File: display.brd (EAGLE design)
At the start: 64.5 x 30.8 mm, 9 parts

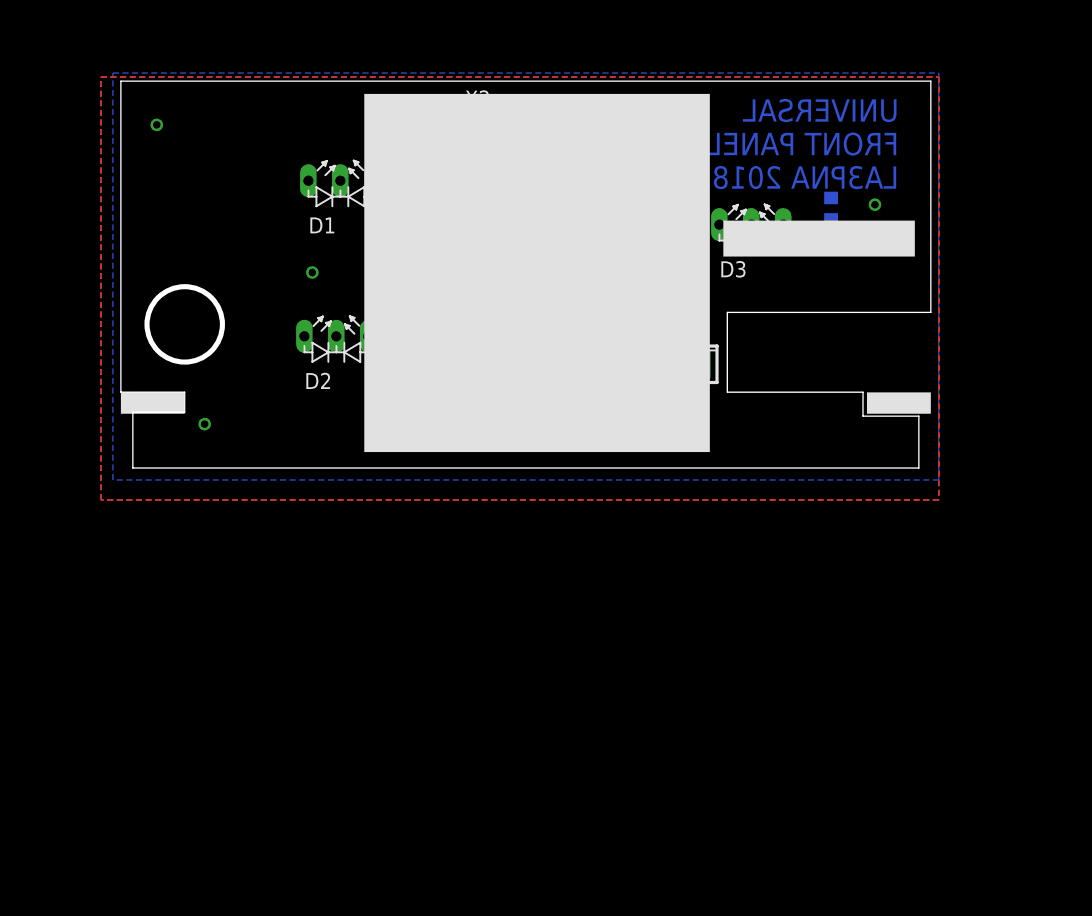
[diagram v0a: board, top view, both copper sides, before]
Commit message: front panel board made to fit
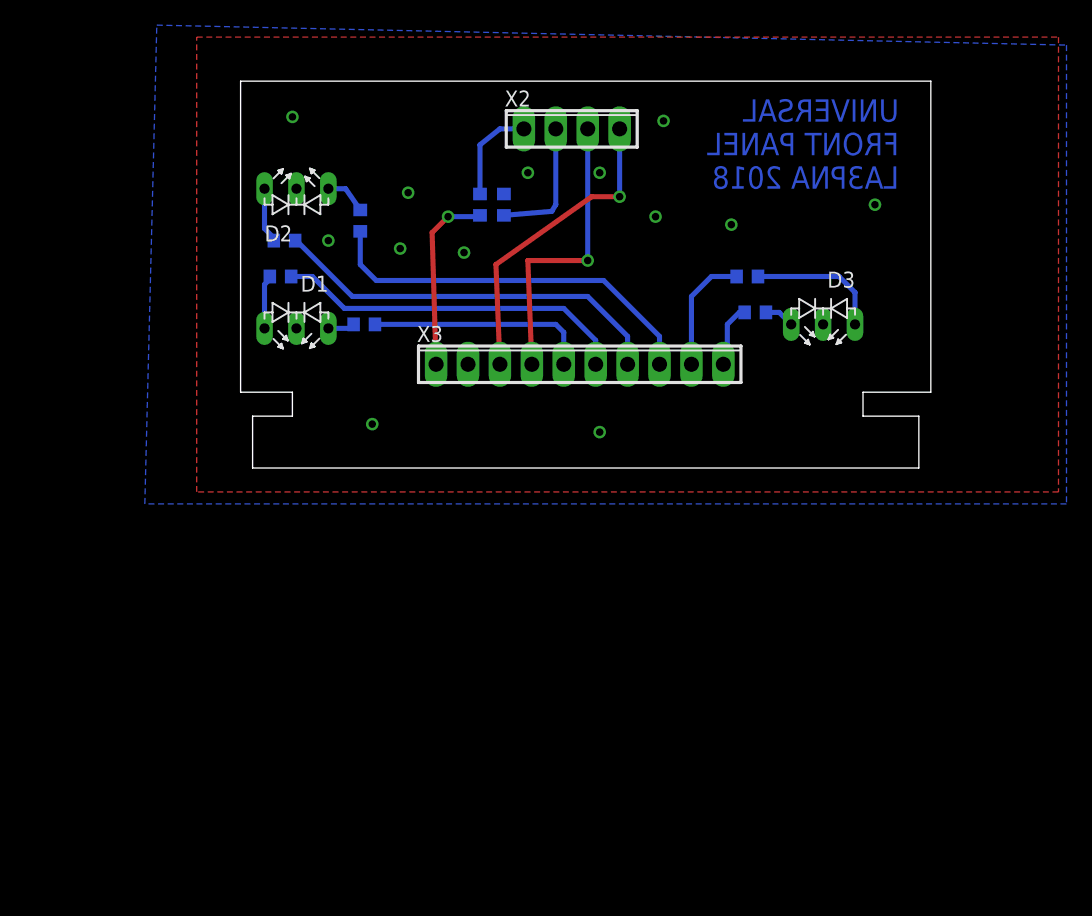
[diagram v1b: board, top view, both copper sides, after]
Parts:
- added R3, R4, R5, R6: 220R, rcl:R0603
- moved R2 44.1 mm to (12.7, 15.2), turned to 180 degrees
- moved R1 25.4 mm to (19.4, 11.4), turned to 0 degrees
- moved D1 13.2 mm to (12.7, 11.1), turned to 180 degrees
- moved D2 12.2 mm to (15.2, 22.2)
- moved D3 8.55 mm to (54.6, 11.4), turned to 180 degrees
- moved X2 3.17 mm to (35.9, 27.0)
- moved X3 1.91 mm to (36.5, 8.26)
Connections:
- new net N$10: D3.A1, R6.2
- new net N$11: R3.1, X3.7
- new net N$12: R4.2, X3.8
- new net N$13: R6.1, X3.9
- new net N$14: R5.2, X3.10
- new net N$5: R1.1, X3.5
- new net N$6: R2.2, X3.6
- new net N$7: D2.A1, R3.2
- new net N$8: D2.A2, R4.1
- new net N$9: D3.A2, R5.1
- net GND: now also D2.K, D3.K
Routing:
- net N$11: track 0.00 -> 31.8 mm
- net N$12: track 0.00 -> 31.0 mm
- net N$6: track 0.00 -> 28.2 mm
- net N$4: track 0.00 -> 24.9 mm, vias 0 -> 1
- net N$3: track 0.00 -> 23.5 mm, vias 0 -> 1
- net N$5: track 0.00 -> 17.8 mm
- net +UB: track 0.00 -> 14.9 mm, vias 0 -> 1
- net N$10: track 0.00 -> 10.8 mm
- net N$13: track 0.00 -> 9.65 mm
- net N$14: track 0.00 -> 5.07 mm
- net N$7: track 0.00 -> 4.43 mm
- net N$2: track 0.00 -> 4.30 mm
- net N$8: track 0.00 -> 3.43 mm
- net N$9: track 0.00 -> 2.40 mm
- net N$15: track 5.50 -> 7.85 mm
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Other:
- board size 64.5 x 30.8 mm -> 54.9 x 30.8 mm

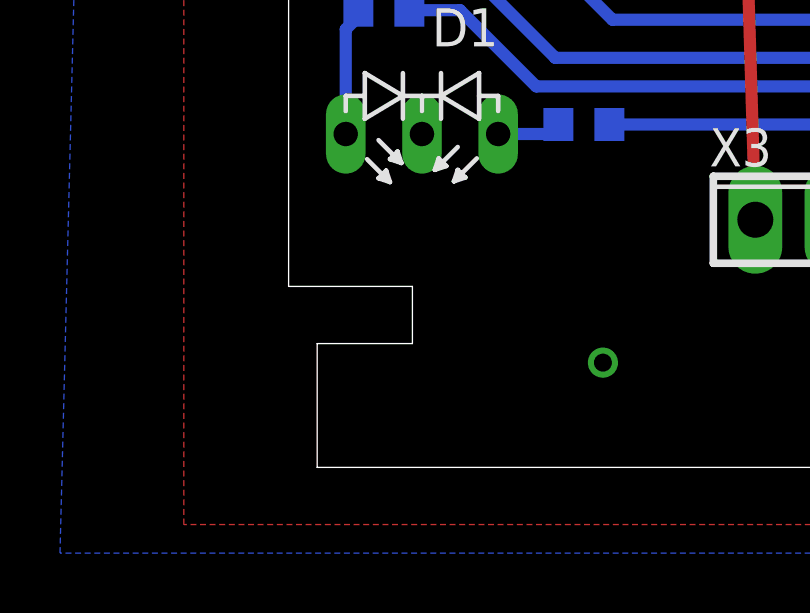
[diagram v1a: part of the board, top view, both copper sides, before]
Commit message: pcb fix
Fix PCB's to make it possible to build the boards without rework
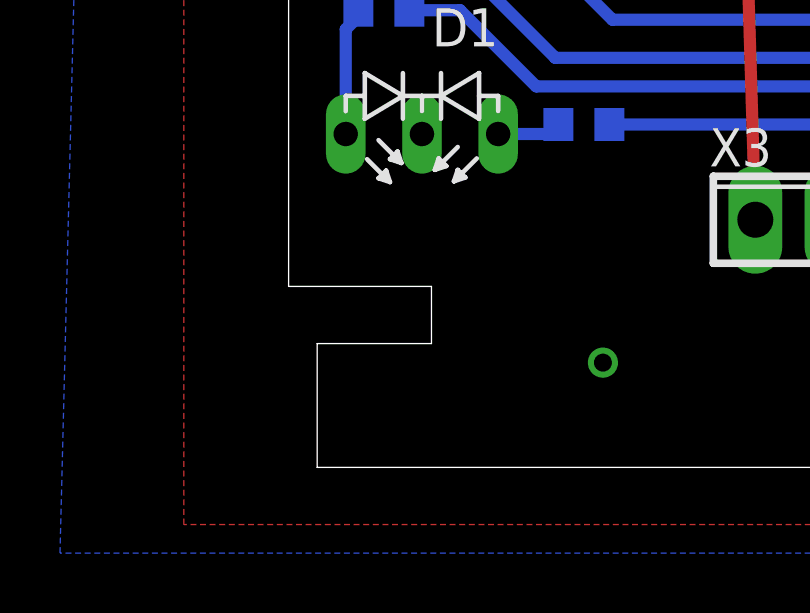
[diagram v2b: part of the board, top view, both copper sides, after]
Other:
- outline, holes or cut-outs redrawn
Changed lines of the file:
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@@
 <wire x1="64.4525" y1="30.785" x2="9.525" y2="30.785" width="0" layer="20"/>
 <wire x1="9.525" y1="30.785" x2="9.525" y2="6.0325" width="0" layer="20"/>
-<wire x1="13.6525" y1="4.1275" x2="10.4775" y2="4.1275" width="0" layer="20"/>
+<wire x1="14.2875" y1="4.1275" x2="10.4775" y2="4.1275" width="0" layer="20"/>
 <wire x1="10.4775" y1="4.1275" x2="10.4775" y2="0" width="0" layer="20"/>
 <text x="61.9125" y="22.225" size="1.778" layer="16" font="vector" rot="MR0">UNIVERSAL
@@
 <dimension x1="59.055" y1="4.1275" x2="36.195" y2="4.1275" x3="47.625" y3="8.5725" textsize="1.778" layer="21"/>
 <dimension x1="13.6525" y1="4.1275" x2="36.5125" y2="4.1275" x3="25.0825" y3="9.140871875" textsize="1.778" layer="25"/>
-<wire x1="9.525" y1="6.0325" x2="13.6525" y2="6.0325" width="0" layer="20"/>
-<wire x1="13.6525" y1="6.0325" x2="13.6525" y2="4.1275" width="0" layer="20"/>
+<wire x1="9.525" y1="6.0325" x2="14.2875" y2="6.0325" width="0" layer="20"/>
+<wire x1="14.2875" y1="6.0325" x2="14.2875" y2="4.1275" width="0" layer="20"/>
 </plain>
 <attributes>

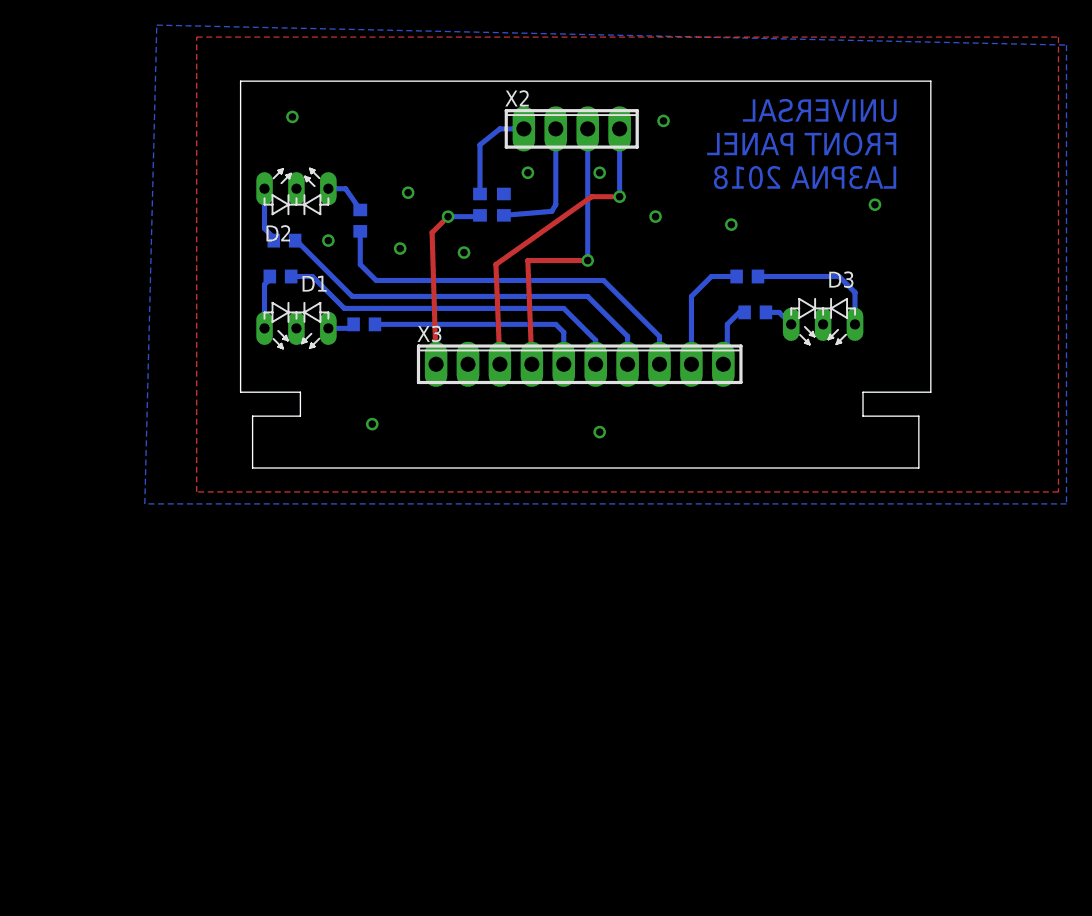
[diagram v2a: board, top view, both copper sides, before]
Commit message: update display.brd and thermocouple
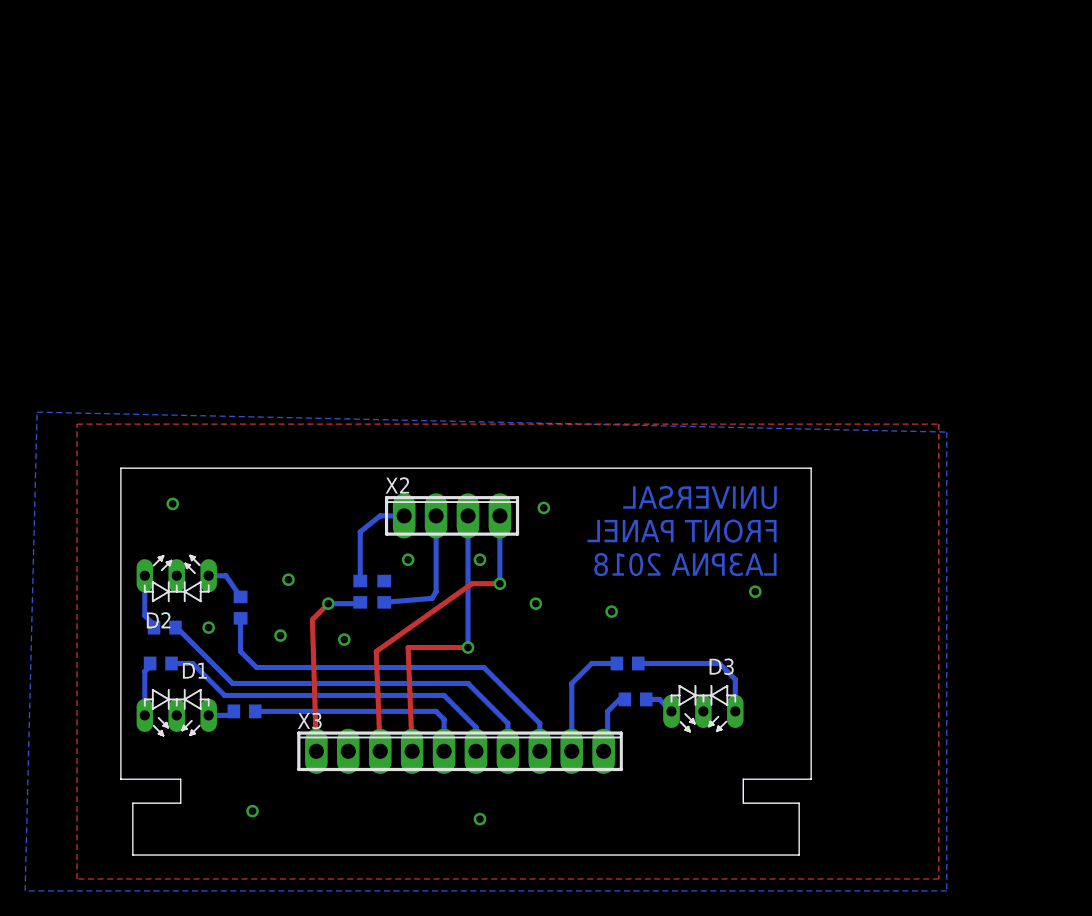
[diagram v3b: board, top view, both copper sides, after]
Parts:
- moved R8 32.2 mm to (21.0, -9.84)
- moved X3 32.2 mm to (27.0, -22.5)
- moved D1 32.2 mm to (3.17, -19.7)
- moved D2 32.2 mm to (5.71, -8.57)
- moved D3 32.2 mm to (45.1, -19.4)
- moved R1 32.2 mm to (9.84, -19.4)
- moved R2 32.2 mm to (3.17, -15.6)
- moved R3 32.2 mm to (3.49, -12.7)
- moved R4 32.2 mm to (9.53, -11.1)
- moved R5 32.2 mm to (41.0, -18.4)
- moved R6 32.2 mm to (40.3, -15.6)
- moved R7 32.2 mm to (19.1, -9.84)
- moved X2 32.2 mm to (26.4, -3.81)
